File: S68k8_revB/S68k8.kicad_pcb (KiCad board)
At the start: 2 copper layers, 160 x 100 mm, 70 parts, among them J1 Connector_DIN41612_2x32, J3 Conn_02x05_Top_Bottom, J4 Conn_02x05_Top_Bottom, U1 ATF16V8C, U10 MC68681P, U11 74LS393, U12 74LS04, U13 27C512, U14 KM62256CLP, U15 KM62256CLP, U16 M48T59, U18 MC1488, U19 MC1489, U2 74LS245, U20 ATF16V8C, U21 MC68008FN, U3 74LS541, U4 74LS244, U5 74LS541, U6 74LS541, U7 74LS07, U8 74LS245, U9 ATF16V8C, Y1 16M, Y2 10M, Y3 3.6864M

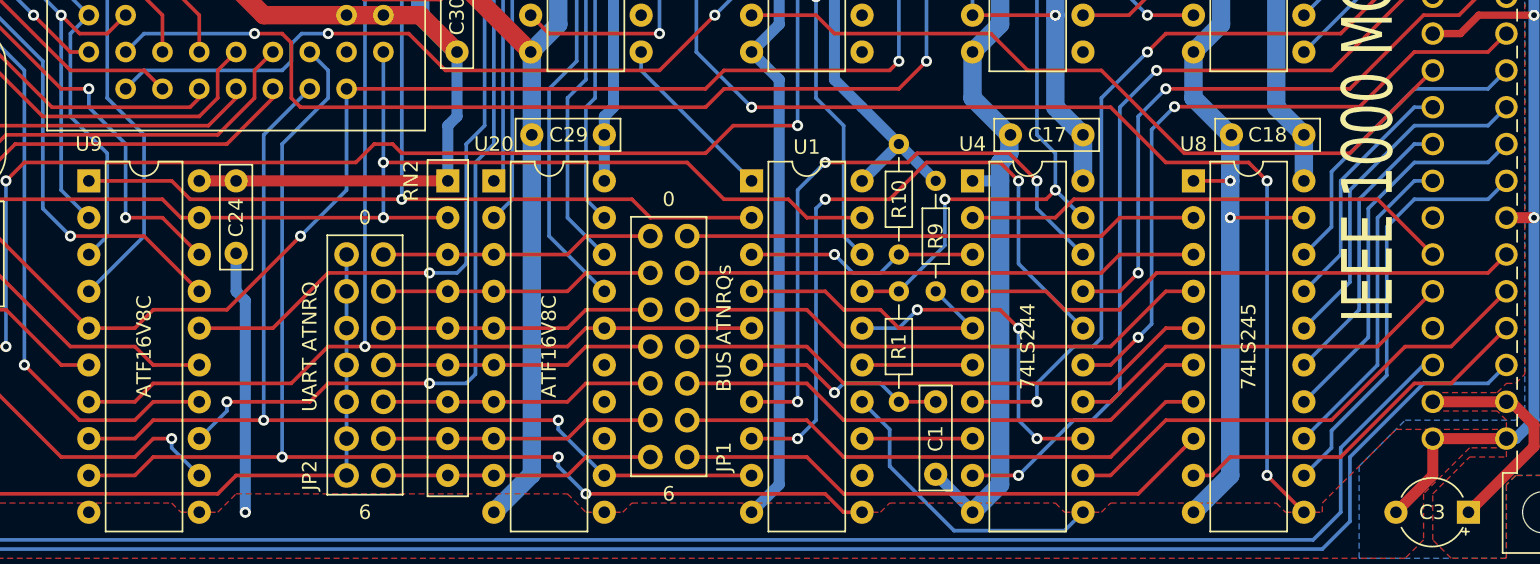
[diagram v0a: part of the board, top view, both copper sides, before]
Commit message: S68k8: change pull-up for DTACK to a separate resistor
Tests show 4k7 is too large to pull the line back fast enough. Reducing to 1k or even 470R give much better results.
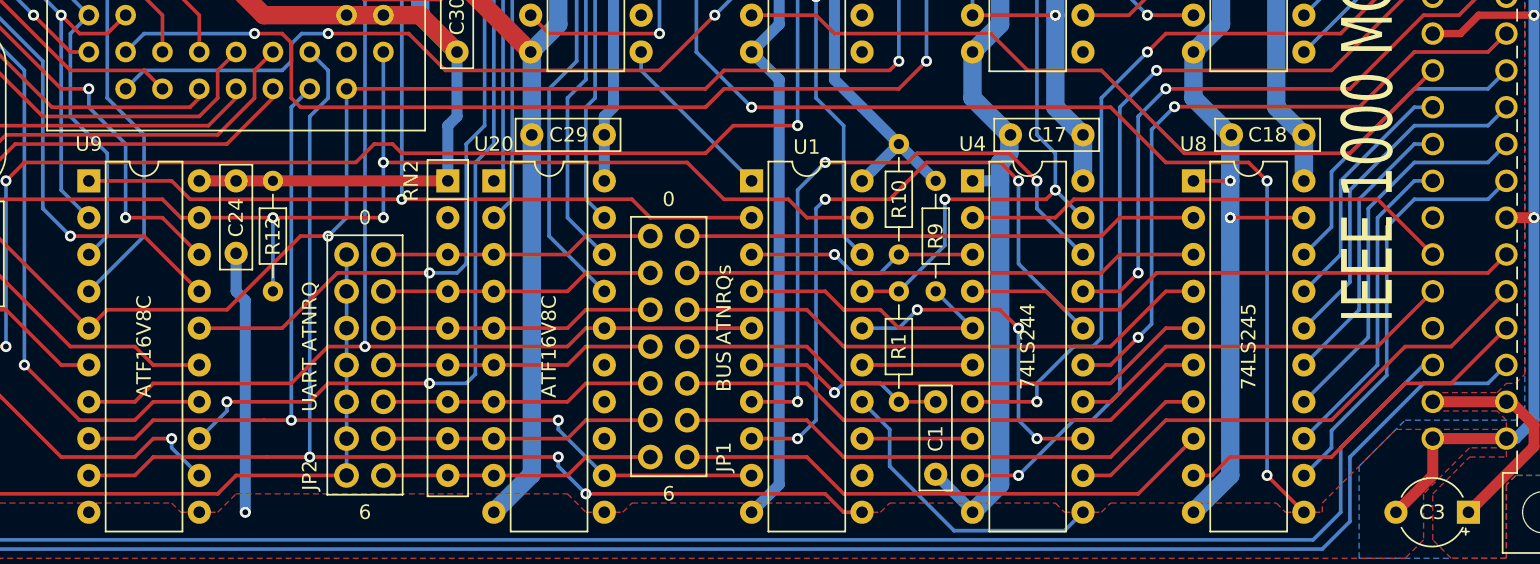
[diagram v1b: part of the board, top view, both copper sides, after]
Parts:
- added R12: 1k, Resistor_THT:R_Axial_DIN0204_L3.6mm_D1.6mm_P7.62mm_Horizontal, F.Cu at (131.7, 116.4)
- R10, R9: value 4k7 -> 1k
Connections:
- RN2 pad 2: ~DTACK -> (no net)
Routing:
- net R~W: track 184.3 -> 185.4 mm
- net ~DS: track 85.6 -> 84.8 mm
- net ~AS: track 72.4 -> 71.6 mm
- net ~DTACK: vias 4 -> 5

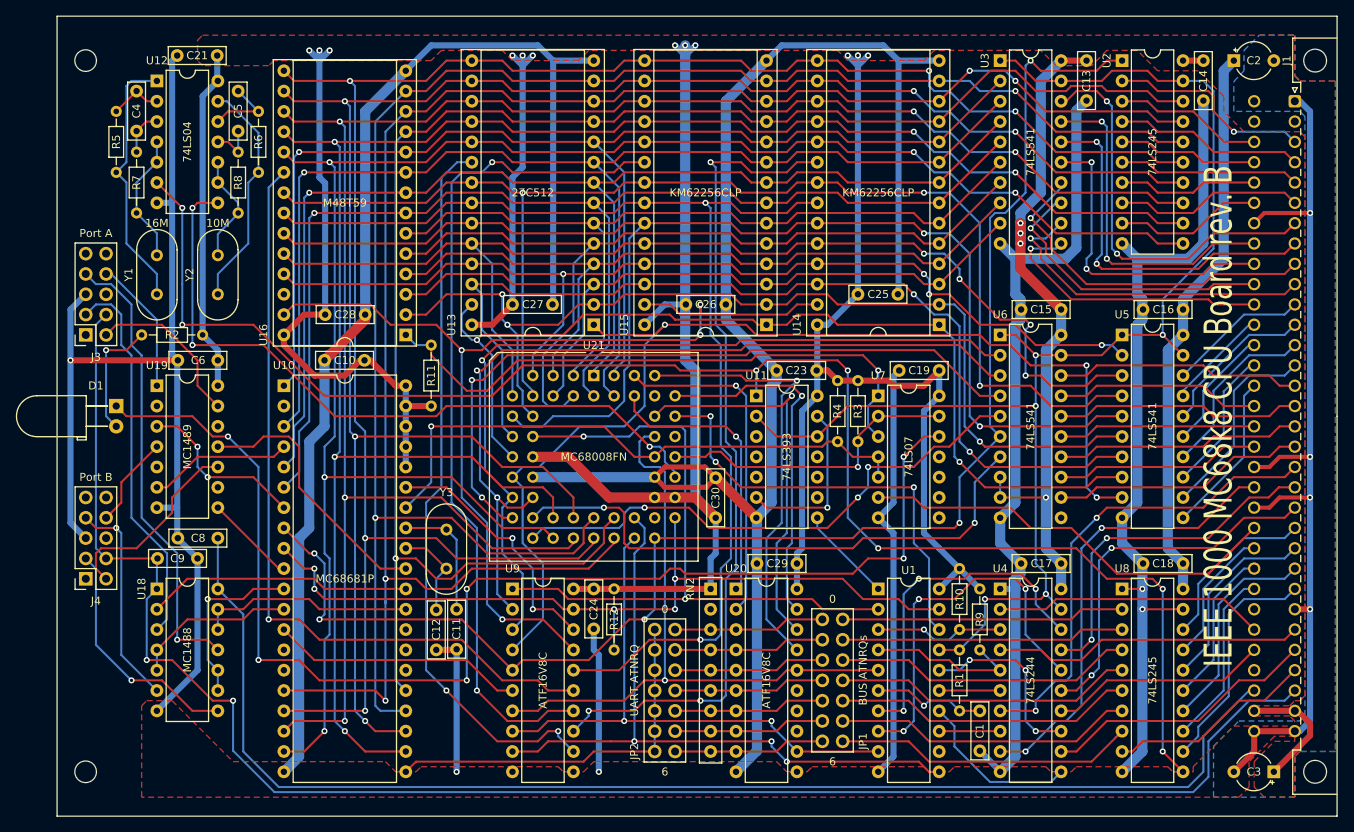
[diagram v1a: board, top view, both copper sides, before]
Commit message: S68k8: moved copper pours for power distribution to the bottom layer
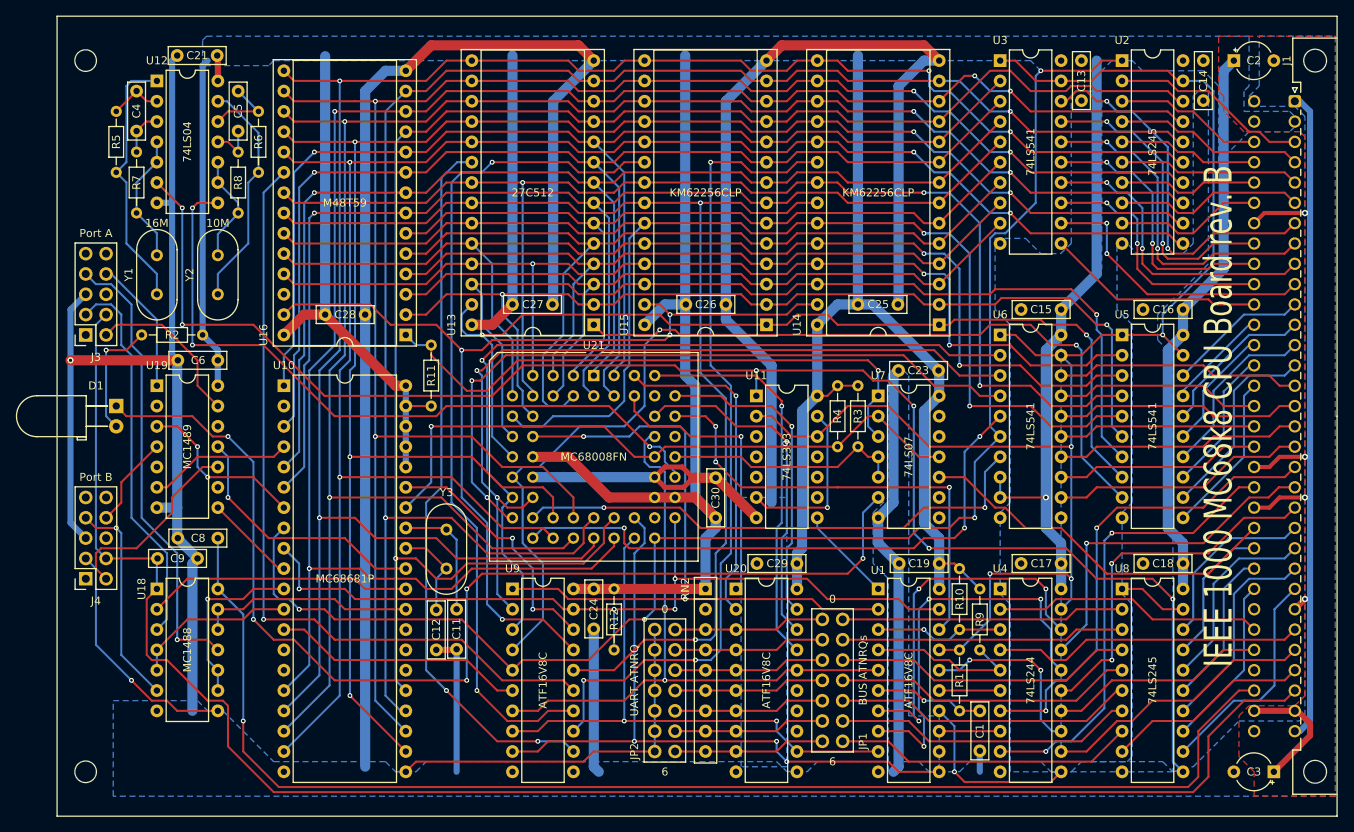
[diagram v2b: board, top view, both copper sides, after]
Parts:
- removed C10: 100n, Capacitor_THT:C_Rect_L7.0mm_W2.0mm_P5.00mm
- moved C19 24.1 mm to (172.3, 113.3)
- moved C23 15.2 mm to (167.2, 89.1)
- moved C25 1.27 mm to (162.2, 80.9)
- moved C13 0.64 mm to (190.1, 50.4)
- moved R3 0.64 mm to (162.2, 91.0)
- moved R4 0.64 mm to (159.6, 91.0)
- moved RN2 0.63 mm to (143.1, 116.4)
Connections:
- U7 pad 10: (no net) -> /STEBUS interface/~STE-SYSRST
- U7 pad 11: (no net) -> ~RESET
- U7 pad 12: Net-(D1-Pad1) -> (no net)
- U7 pad 13: ~HALT -> (no net)
- U7 pad 2: ~HALT -> ~RESET
- U7 pad 4: ~RESET -> ~HALT
- U7 pad 5: ~RESET -> ~HALT
- U7 pad 6: /STEBUS interface/~STE-SYSRST -> Net-(D1-Pad1)
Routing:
- net GND: track 887.3 -> 640.1 mm, vias 9 -> 5
- net +5V: track 583.5 -> 554.8 mm, vias 16 -> 1
- net Net-(D1-Pad1): track 158.5 -> 140.5 mm, vias 6 -> 5
- net ~BUSEN: track 177.1 -> 189.4 mm, vias 5 -> 4
- net /STEBUS interface/STE-A7: track 35.7 -> 27.3 mm, vias 1 -> 0
- net ~HALT: track 38.3 -> 30.0 mm, vias 1 -> 0
- net ~RESET: track 73.1 -> 80.8 mm
- net /STEBUS interface/~STE-SYSRST: track 53.3 -> 46.7 mm
- net D4: track 238.5 -> 232.1 mm, vias 5 -> 4
- net ~MEMWE: track 129.7 -> 123.4 mm
- net /STEBUS interface/STE-A6: track 41.8 -> 35.7 mm, vias 1 -> 2
- net D6: track 236.7 -> 230.7 mm
- net /CPU complex/~IPL1: track 49.2 -> 43.4 mm
- net /STEBUS interface/STE-A4: track 44.3 -> 38.6 mm, vias 1 -> 2
- net /CPU complex/~IPL0: track 54.9 -> 49.6 mm
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- added copper zone on B.Cu, net +5V
- removed copper zone on F.Cu, net GND
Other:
- net class Default: via_dia 0.762 -> 0.61; via_drill 0.4 -> 0.32
